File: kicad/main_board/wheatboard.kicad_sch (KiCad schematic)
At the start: 0 parts

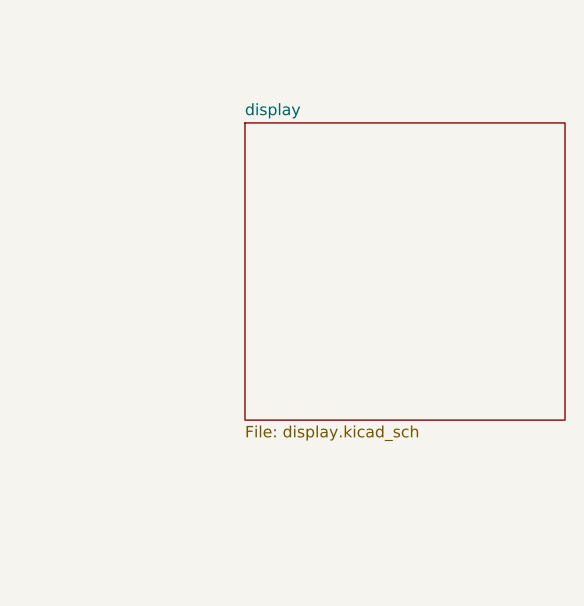
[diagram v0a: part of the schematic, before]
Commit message: separate main board and daughter board
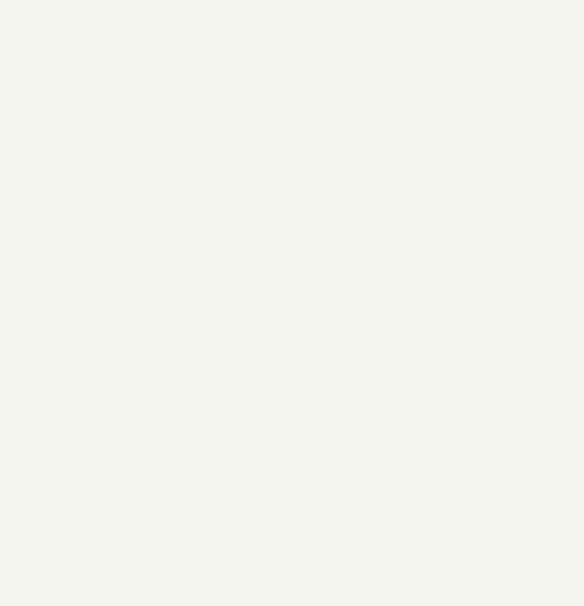
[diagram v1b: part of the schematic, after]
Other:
- removed sheet display
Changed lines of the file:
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@@
-		)
-	)
-	(sheet
-		(at 211.455 45.72)
-		(size 35.56 33.02)
-		(exclude_from_sim no)
-		(in_bom yes)
-		(on_board yes)
-		(dnp no)
-		(fields_autoplaced yes)
-		(stroke
-			(width 0.1524)
-			(type solid)
-		)
-		(fill
-			(color 0 0 0 0.0000)
-		)
-		(property "Sheetname" "display"
-			(at 211.455 45.0084 0)
-			(effects
-				(font
-					(size 1.27 1.27)
-				)
-				(justify left bottom)
-			)
-		)
-		(property "Sheetfile" "display.kicad_sch"
-			(at 211.455 79.3246 0)
-			(effects
-				(font
-					(size 1.27 1.27)
-				)
-				(justify left top)
-			)
-		)
-		(instances
-			(project "wheatboard"
-				(path "/6dbb65f4-5576-4e18-9627-83014d84ecc4"
-					(page "7")
-				)
-			)
 		)
 	)
